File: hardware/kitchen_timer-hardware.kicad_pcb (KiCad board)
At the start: 2 copper layers, 60 x 114.3 mm, 80 parts, among them J1 Conn_01x02, J2 Conn_01x02_Pin, J3 AVR-ISP-6, Q1 JSM2302, Q2 IRLML6402, Q3 MMBT3904, SW2 SKRPACE010, U1 CH340E UART Module, U10 MAX7219, U11 KWM-20882CUYB, U12 KWM-20882CUYB, U13 KWM-20882CUYB, U14 KWM-20882CUYB, U2 TP4056 breakout, U3 SparkFun_LiPower, U5 ATMEGA328P-AU, U6 PEC11R-4215F-S0024, U7 MAX7219, U8 MAX7219, U9 MAX7219, Y1 Crystal-32kHz

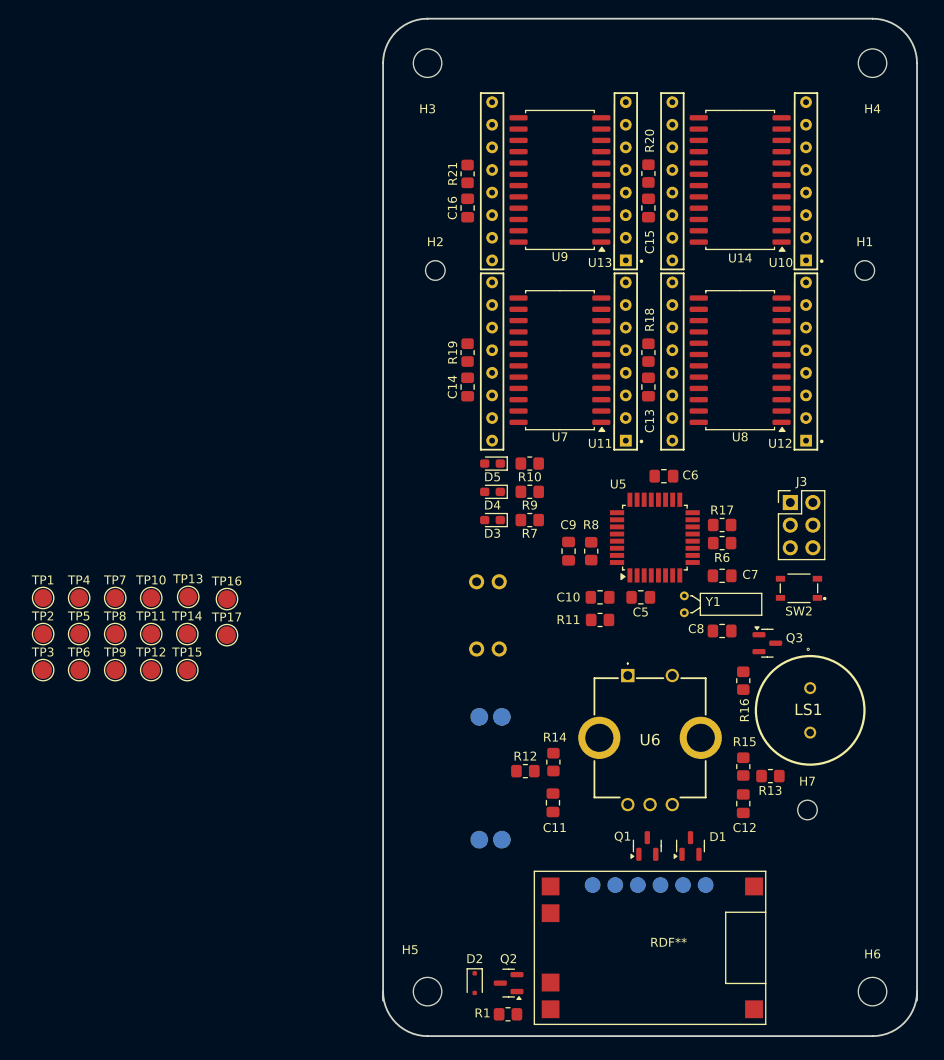
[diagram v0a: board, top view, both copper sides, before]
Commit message: I shorten the leads on the buzzer 3d model
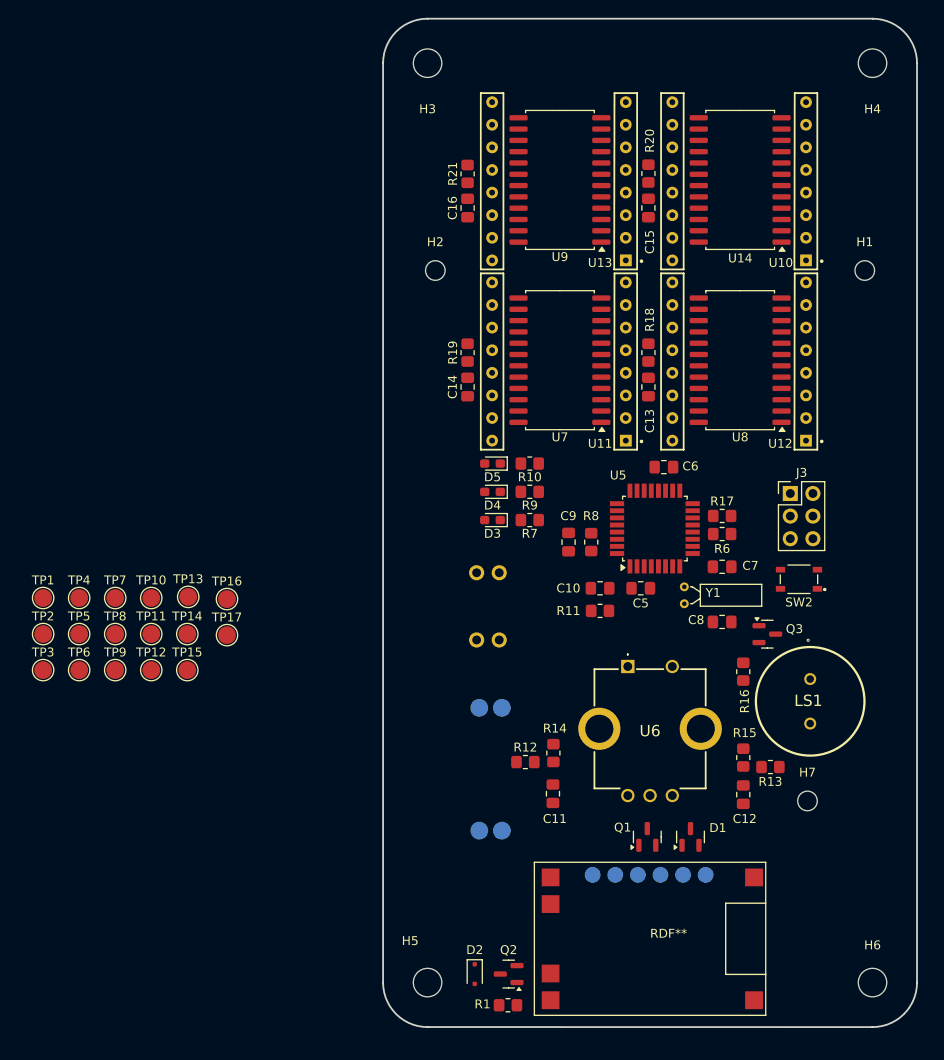
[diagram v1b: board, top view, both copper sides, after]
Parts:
- moved U1 1.14 mm to (148.8, 138.3)
- moved U2 1.02 mm to (157.0, 128.8)
- moved C10 1.02 mm to (151.4, 89.4)
- moved C12 1.02 mm to (167.5, 112.6)
- moved C5 1.02 mm to (156.0, 89.4)
- moved C6 1.02 mm to (158.6, 75.8)
- moved C7 1.02 mm to (165.1, 87.0)
- moved C8 1.02 mm to (165.1, 93.2)
- moved C9 1.02 mm to (147.8, 84.2)
- moved D1 1.02 mm to (161.5, 117.3)
- moved H7 1.02 mm to (174.7, 113.3)
- moved J1 1.02 mm to (135.1, 85.4)
- moved J2 1.02 mm to (135.1, 92.9)
- moved J3 1.02 mm to (172.8, 78.8)
- moved Q1 1.02 mm to (156.7, 117.3)
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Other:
- board size 60 x 114.3 mm -> 60 x 113.3 mm

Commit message: I routed the display, added the SPI Test Points. Before calling it a day, I runned Rules Check and fixed all the issues related to display routing, text size and some issues with the footprints.
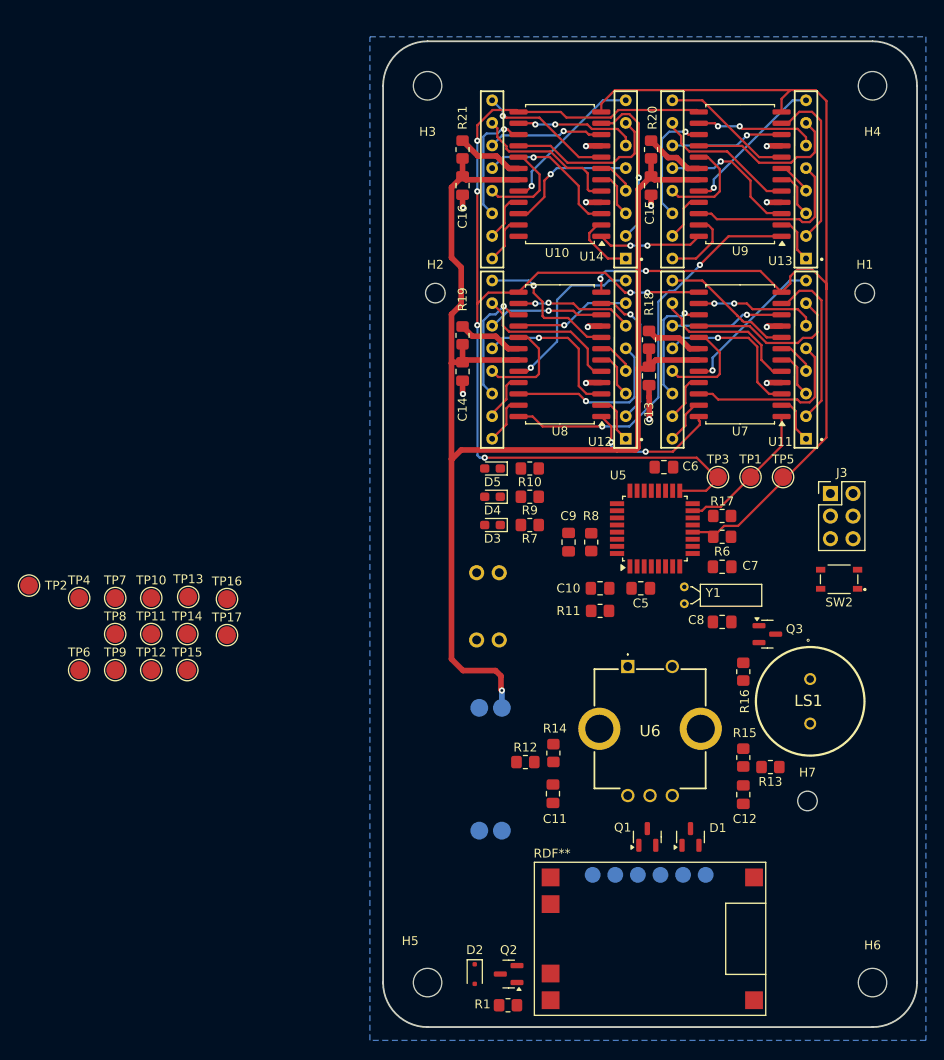
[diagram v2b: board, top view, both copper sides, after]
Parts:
- moved TP5 81.0 mm to (171.9, 76.9)
- moved TP1 80.6 mm to (168.3, 76.9)
- moved TP3 78.9 mm to (164.6, 76.9)
- moved U10 20.3 mm to (146.9, 42.9)
- moved U7 20.3 mm to (167.1, 63.1)
- moved U8 20.3 mm to (146.9, 63.1)
- moved U9 20.3 mm to (167.1, 42.9)
- moved U11 20.3 mm to (167.1, 63.7)
- moved U12 20.3 mm to (146.9, 63.7)
- moved U13 20.3 mm to (167.1, 43.5)
- moved U14 20.3 mm to (146.9, 43.5)
- moved TP2 5.67 mm to (87.2, 89.1)
- moved J3 4.51 mm to (177.3, 78.8)
- moved SW2 4.51 mm to (178.2, 88.4)
- moved R21 2.80 mm to (135.9, 40.1)
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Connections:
- U1 pad 1: Net-(Q1-S) -> unconnected-(U1-+3.3V-Pad1)
- U1 pad 2: Net-(D1-A) -> /Microcontroller/DTR
- U1 pad 3: /Microcontroller/DTR -> Net-(Q1-S)
- U1 pad 4: /BMS & Power Path/+5V-USB -> Net-(D1-A)
- U1 pad 5: unconnected-(U1-+3.3V-Pad5) -> /BMS & Power Path/+5V-USB
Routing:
- net +5V: track 0.00 -> 153.2 mm, vias 0 -> 1
- net /LED Matrices Drivers/SCK: track 0.00 -> 123.7 mm, vias 0 -> 6
- net /LED Matrices Drivers/CS: track 0.00 -> 119.4 mm, vias 0 -> 2
- net Net-(U8-DOUT): track 0.00 -> 45.2 mm, vias 0 -> 2
- net GND: track 0.00 -> 21.5 mm, vias 0 -> 12
- net /LED Matrices Drivers/Mat1A.SEG_DP: track 0.00 -> 19.6 mm
- net /LED Matrices Drivers/Mat1B.SEG_DP: track 0.00 -> 19.6 mm, vias 0 -> 1
- net /LED Matrices Drivers/Mat2A.SEG_DP: track 0.00 -> 19.6 mm
- net /LED Matrices Drivers/Mat1A.DIG_1: track 0.00 -> 19.3 mm
- net /LED Matrices Drivers/Mat2A.DIG_1: track 0.00 -> 19.0 mm
- net /LED Matrices Drivers/Mat1B.SEG_C: track 0.00 -> 19.0 mm, vias 0 -> 1
- net /LED Matrices Drivers/Mat1A.SEG_B: track 0.00 -> 18.4 mm
- net /LED Matrices Drivers/Mat2B.DIG_1: track 0.00 -> 18.3 mm, vias 0 -> 1
- net /LED Matrices Drivers/Mat2B.SEG_B: track 0.00 -> 18.1 mm
- net /LED Matrices Drivers/Mat2A.SEG_B: track 0.00 -> 18.0 mm
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- added copper zone on B.Cu, net GND
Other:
- board size 60 x 113.3 mm -> 60 x 110.8 mm

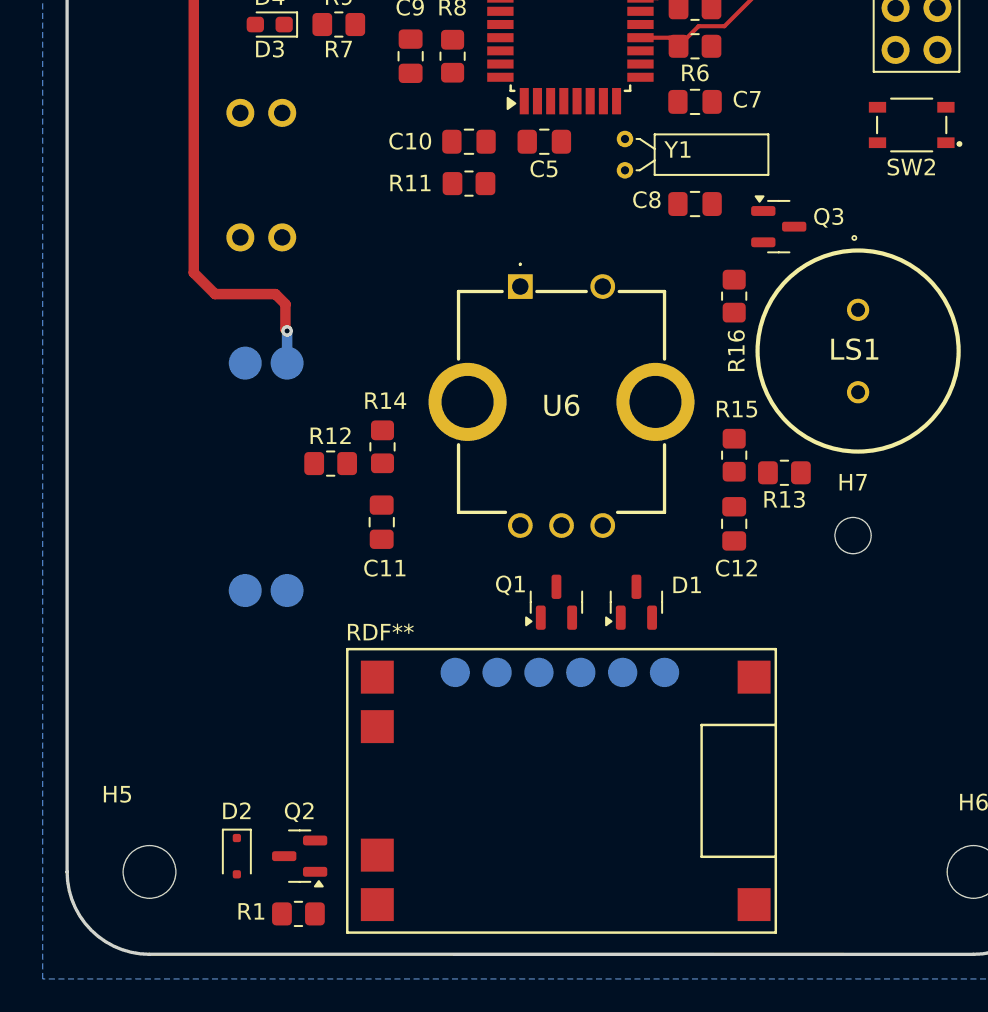
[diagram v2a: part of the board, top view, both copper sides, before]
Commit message: Move connectors a lot closer to their use
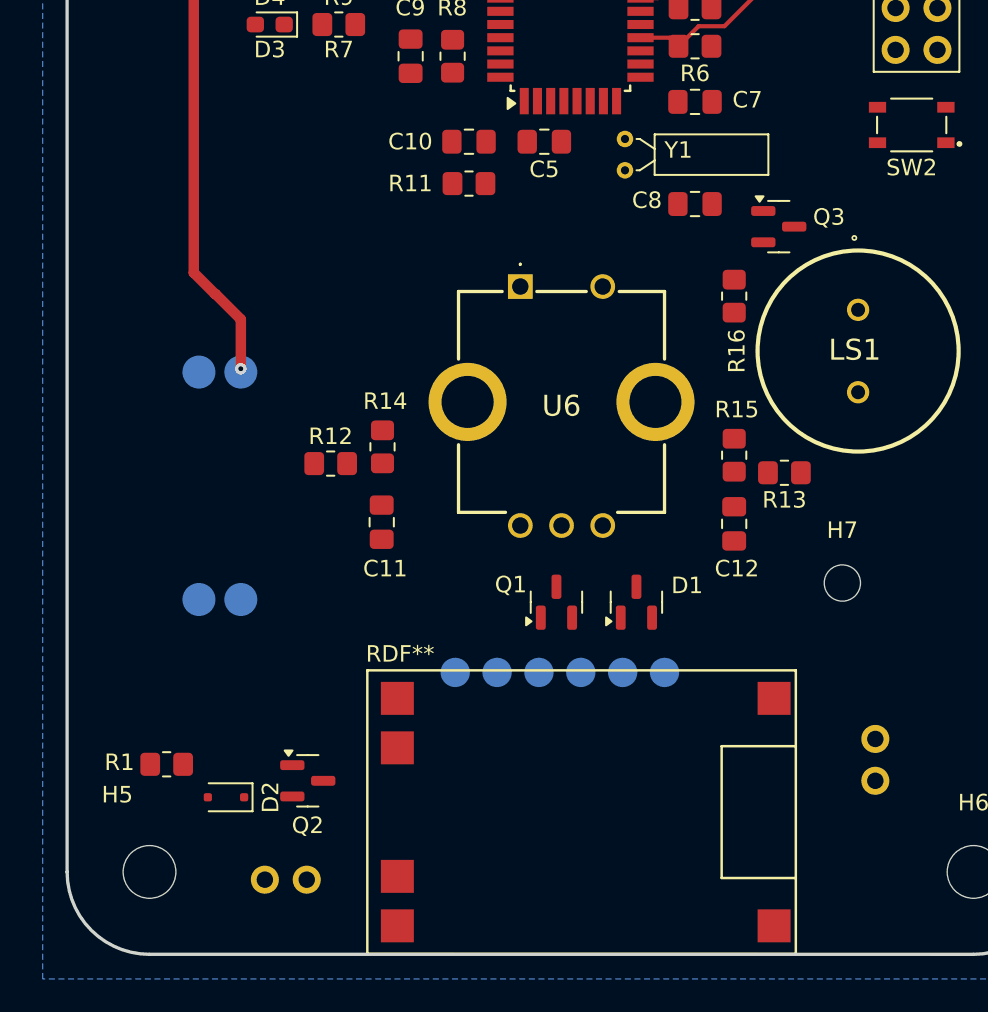
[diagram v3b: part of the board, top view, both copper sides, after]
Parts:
- moved J1 57.5 mm to (178.3, 123.2), turned to -90 degrees
- moved J2 39.0 mm to (136.6, 131.9)
- moved R1 12.1 mm to (133.0, 127.2)
- moved Q2 4.60 mm to (141.6, 128.2), turned to 0 degrees
- moved D2 3.63 mm to (136.6, 129.2), turned to 180 degrees
- moved H7 2.95 mm to (174.0, 116.2)
- moved U3 2.86 mm to (136.3, 115.4)
- moved U2 1.77 mm to (158.2, 130.1)
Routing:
- net +5V: track 153.2 -> 150.4 mm

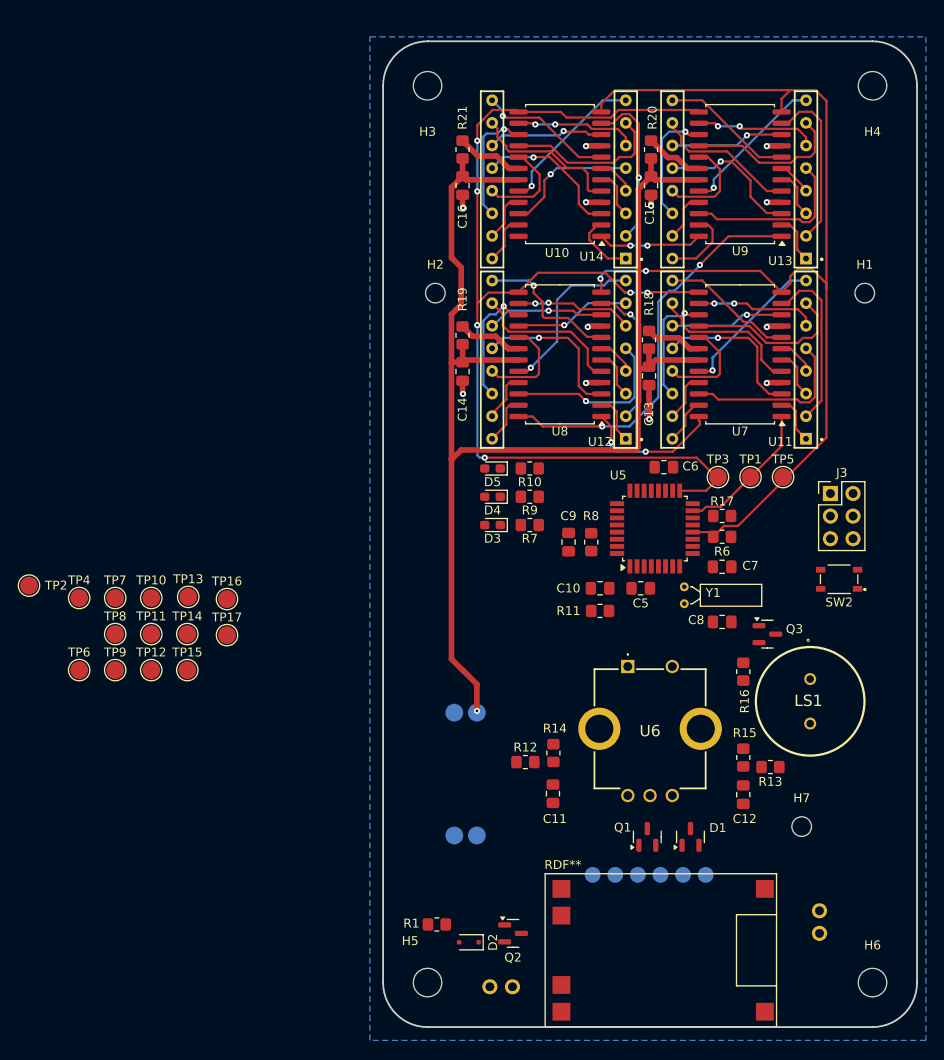
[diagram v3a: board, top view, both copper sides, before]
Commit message: Routed most small components
WIP on SPI
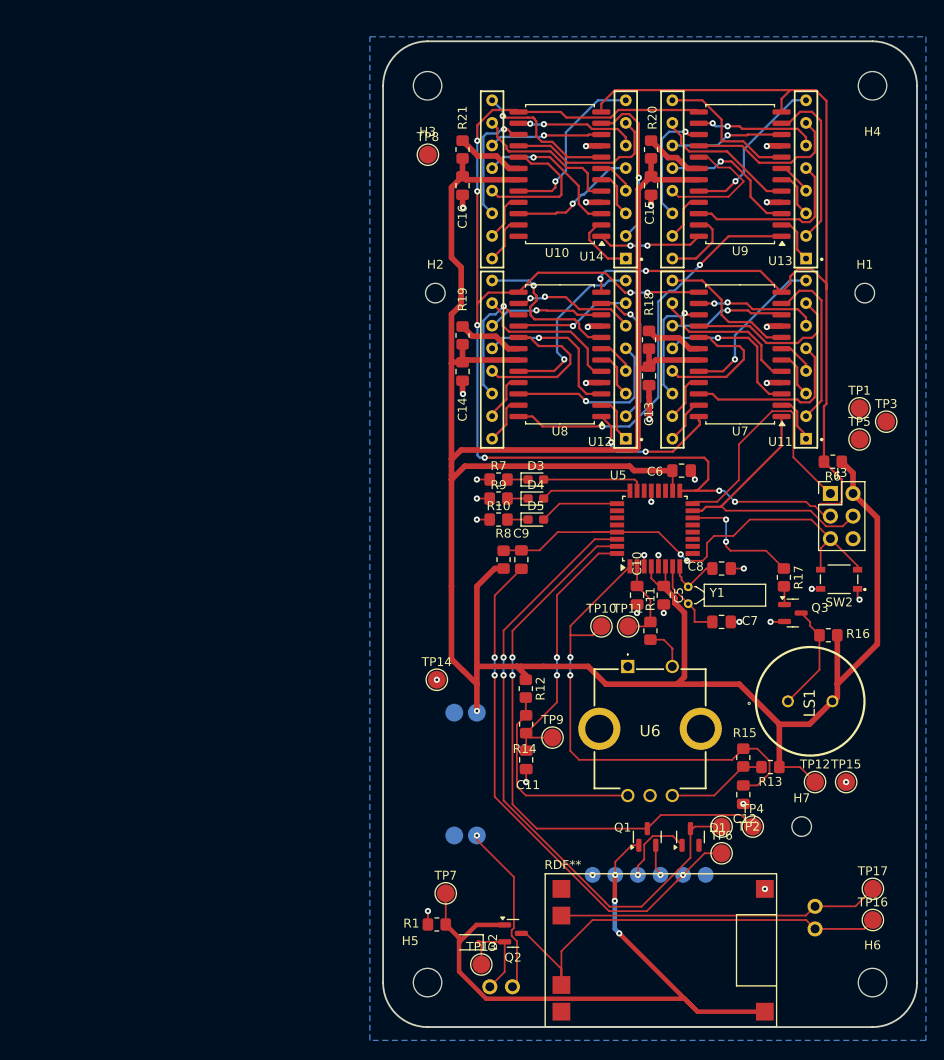
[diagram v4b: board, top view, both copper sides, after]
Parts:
- moved TP2 82.4 mm to (165.0, 116.2)
- moved TP16 81.0 mm to (182.0, 126.7)
- moved TP4 79.9 mm to (168.5, 116.2)
- moved TP17 78.0 mm to (182.0, 123.2)
- moved TP12 75.6 mm to (175.5, 111.2)
- moved TP15 75.1 mm to (179.0, 111.2)
- moved TP6 75.1 mm to (165.0, 119.2)
- moved TP8 64.3 mm to (132.0, 40.7)
- moved TP11 53.6 mm to (154.5, 93.7)
- moved TP13 52.8 mm to (138.0, 131.7)
- moved TP10 50.7 mm to (151.5, 93.7)
- moved TP7 49.8 mm to (134.0, 123.7)
- moved TP9 49.7 mm to (146.0, 106.2)
- moved TP14 28.5 mm to (133.0, 99.7)
- moved TP3 19.9 mm to (183.5, 70.7)
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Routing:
- net +5V: track 150.4 -> 303.8 mm
- net /BMS & Power Path/+5V-USB: track 0.00 -> 76.3 mm, vias 0 -> 3
- net /Microcontroller/MCU_RXD: track 0.00 -> 71.4 mm, vias 0 -> 2
- net /Microcontroller/MCU_TXD: track 0.00 -> 64.5 mm, vias 0 -> 2
- net /Microcontroller/DTR: track 0.00 -> 61.3 mm, vias 0 -> 3
- net /Microcontroller/ENCODER_CH_B: track 0.00 -> 56.2 mm, vias 0 -> 2
- net /Microcontroller/RESET: track 0.00 -> 54.8 mm, vias 0 -> 2
- net /BMS & Power Path/BAT+: track 0.00 -> 49.0 mm
- net /BMS & Power Path/BAT-: track 0.00 -> 36.2 mm
- net /Microcontroller/ENCODER_CH_A: track 0.00 -> 30.8 mm, vias 0 -> 2
- net /Microcontroller/MISO: track 0.00 -> 29.0 mm
- net Net-(U6-CHANNEL_A): track 0.00 -> 23.3 mm
- net GND: track 21.5 -> 42.1 mm, vias 12 -> 33
- net /+5V Boost Converter/PP_VCC_after_switch: track 0.00 -> 19.3 mm, vias 0 -> 1
- net /LED Matrices Drivers/MOSI: track 16.3 -> 33.1 mm
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
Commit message: Rotate BMS and add some small adjustments to fix some DRC issues
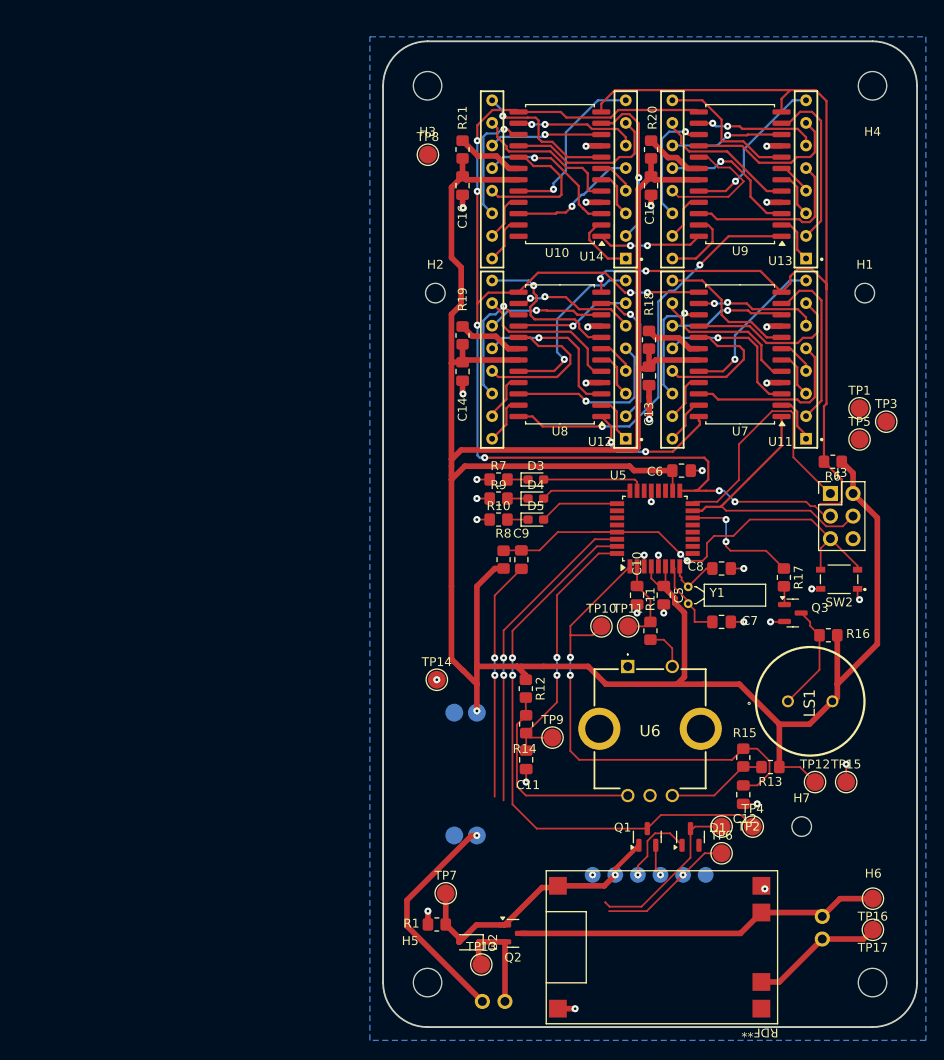
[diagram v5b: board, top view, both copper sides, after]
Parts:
- moved J2 9.06 mm to (143.1, 138.1), turned to 180 degrees
- moved J1 8.28 mm to (178.7, 123.9), turned to -90 degrees
- moved TP17 4.60 mm to (182.0, 127.8), turned to 180 degrees
- moved TP16 2.40 mm to (182.0, 124.3), turned to 180 degrees
- moved U2 0.36 mm to (158.3, 129.7), turned to 0 degrees
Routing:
- net /BMS & Power Path/+5V-USB: track 76.3 -> 31.3 mm, vias 3 -> 1
- net /BMS & Power Path/BAT-: track 36.2 -> 15.0 mm
- net /Microcontroller/DTR: track 61.3 -> 43.1 mm
- net /Microcontroller/MCU_RXD: track 71.4 -> 55.3 mm
- net /BMS & Power Path/BAT+: track 49.0 -> 41.5 mm
- net /+5V Boost Converter/PP_VCC_after_switch: track 19.3 -> 25.8 mm
- net GND: track 42.1 -> 48.1 mm
- net +5V: track 303.8 -> 302.4 mm
- net /+5V Boost Converter/PP_VCC: track 11.3 -> 12.3 mm
- net unconnected-(U2-OUT+-Pad3): vias 0 -> 1
